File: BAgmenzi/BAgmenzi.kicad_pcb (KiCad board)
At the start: 6 copper layers, 66.2 x 44.8 mm, 146 parts, among them IC1 TPL0501-100RSER, J1 Conn_01x07, J2 DF52-2S-0.8H(21), J3 USB3076-30-A, J4 connector for CMUT, J5 3220-10-0100-00, Q1 NX7002BKMBYL, U1 MSP430FR5043IRGCT, U10 PESD1USB30, U11 MAX77654BENV+T, U13 TPS7A2033DBVDQN, U2 AD8338ACPZ-R7, U3 OPA836IDBVT, U4 OPA836IDBVT, U7 LT3463AEDD#PBF, U8 TPS22916CYFPR, U9 MAXM86161EFD_T, X1 FY0800018, X2 ABS07-32.768KHZ-9-T, Y1 AWSCR-8.00CV-T

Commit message: DRC correfted all red falgs
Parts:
- added TP2: vga_vref, TestPoint:TestPoint_Pad_D2.0mm, F.Cu at (192.8, 108.0)
- added TP6: TestPoint, TestPoint:TestPoint_Pad_D2.0mm, F.Cu at (192.8, 112.1)
- moved D4 1.02 mm to (127.6, 119.6)
- moved J3 0.78 mm to (122.5, 118.4)
- moved X2 0.54 mm to (125.6, 113.0)
- moved C16 0.53 mm to (123.9, 114.0)
- moved C18 0.52 mm to (123.9, 112.0)
- moved C50 0.46 mm to (150.5, 102.4), turned to 0 degrees
- moved R11 0.24 mm to (140.5, 95.7)
- moved X1 0.17 mm to (124.6, 118.4)
- moved C7 0.12 mm to (128.5, 109.2)
- moved R14 0.10 mm to (150.0, 116.4)
- turned R17 to 90 degrees
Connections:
- R17 pad 1: unconnected-(R17-Pad1) -> /TX/PULSER_IN
- R17 pad 2: unconnected-(R17-Pad2) -> PULSE_OUT
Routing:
- net GND: track 89.8 -> 137.5 mm, vias 67 -> 102
- net CHGIN: track 2.16 -> 45.1 mm, vias 0 -> 2
- net DVDD_3.3: track 56.1 -> 76.5 mm, vias 13 -> 23
- net PULSE_OUT: track 0.00 -> 17.7 mm, vias 0 -> 2
- net PULSER_HIZ_IN: track 0.99 -> 8.47 mm
- net Net-(C53-Pad1): track 0.40 -> 5.98 mm, vias 0 -> 2
- net /MSP/AVCC1: track 2.73 -> 5.85 mm
- net PPG_INT: track 81.1 -> 83.0 mm
- net DATA_READY: track 33.3 -> 31.6 mm
- net /TX/PULSER_EN: track 0.00 -> 1.65 mm
- net PPG_I2C.SCL: track 93.4 -> 94.9 mm
- net V_BAT: track 10.5 -> 9.26 mm, vias 3 -> 4
- net PMIC_IRQ: track 32.0 -> 33.2 mm
- net /MSP/LFXOUT: track 6.56 -> 5.44 mm
- net PPG_GPIO: track 66.0 -> 67.1 mm
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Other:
- board size 66.2 x 44.8 mm -> 64.7 x 44.8 mm

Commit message: added polyCMUT footprint, changed enables, more compact
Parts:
- removed J4: connector for CMUT, cmut_dummy:cmut-dummy
- removed TP2: vga_vref, TestPoint:TestPoint_Pad_D2.0mm
- removed TP6: TestPoint, TestPoint:TestPoint_Pad_D2.0mm
- added C67: 47u, Capacitor_SMD:C_0402_1005Metric, F.Cu at (146.6, 104.4)
- added R2: 1M, Resistor_SMD:R_0402_1005Metric, F.Cu at (144.3, 108.2)
- added R3: 1M, Resistor_SMD:R_0402_1005Metric, F.Cu at (142.9, 109.1)
- added R47: 1k, Resistor_SMD:R_0402_1005Metric, B.Cu at (125.5, 107.7)
- added R48: 1k, Resistor_SMD:R_0402_1005Metric, B.Cu at (124.5, 107.2)
- added U5: polyCMUT, polyCMUT:polyCMUT, F.Cu at (162.8, 108.8)
- C25: value 10nF -> 1.5n
- C34: value 1n -> 3.3n
- R10: value 100 -> 0
- R11: value 400 -> 1
- R7: value 2k -> 200
- R8: value 2k -> 1k
- moved R41 25.2 mm to (159.0, 95.7), turned to 180 degrees
- moved JP2 25.1 mm to (161.5, 97.9), turned to 90 degrees
- moved JP4 22.3 mm to (157.4, 97.6)
- moved R43 18.2 mm to (156.2, 99.7)
- moved C61 18.2 mm to (158.7, 99.7)
- moved R6 9.99 mm to (137.0, 115.1)
- moved C63 9.67 mm to (159.2, 120.9)
- moved JP5 9.67 mm to (157.4, 118.5)
- moved R44 9.67 mm to (155.9, 120.7)
- moved C62 9.67 mm to (157.7, 121.0)
- moved JP1 6.64 mm to (147.5, 118.3), turned to -90 degrees
- moved R30 4.88 mm to (166.3, 119.0)
- moved R29 4.84 mm to (166.3, 117.8)
- moved R27 4.39 mm to (169.4, 118.0)
- moved R28 4.24 mm to (169.4, 119.2)
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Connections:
- M1 pad F2: HV_PWR_EN -> Net-(M1-P115)
- M1 pad F3: VRX_EN -> Net-(M1-P114)
- M1 pad H5: HV_POS_EN -> BSL.UART_RX
- M1 pad H6: HV_NEG_EN -> BSL.UART_TX
- U1 pad 20: unconnected-(U1-P1.3_UCA1SOMI_UCA1RXD_TA1.1_A9_C9-Pad20) -> VRX_EN
- U1 pad 50: unconnected-(U1-P3.3_MCLK_TB0.3_XPB1-Pad50) -> HV_POS_EN
- U1 pad 51: unconnected-(U1-P3.4_SMCLK_DMAE0-Pad51) -> HV_NEG_EN
- U1 pad 52: unconnected-(U1-P3.5_ACLK_COUT-Pad52) -> HV_PWR_EN
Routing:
- net BSL.UART_TX: track 12.6 -> 38.6 mm, vias 0 -> 2
- net BSL.UART_RX: track 17.2 -> 40.8 mm, vias 0 -> 2
- net VRX_EN: track 32.8 -> 13.8 mm, vias 0 -> 1
- net HV_PWR_EN: track 43.1 -> 26.3 mm
- net HV_POS_EN: track 28.0 -> 12.5 mm, vias 0 -> 2
- net RX_IN: track 1.31 -> 14.5 mm
- net JTAG.RESET_N: track 29.6 -> 41.1 mm, vias 0 -> 2
- net Net-(M1-P115): track 0.00 -> 10.7 mm
- net PPG_I2C.SCL: track 94.9 -> 84.8 mm
- net HV_NEG_EN: track 27.3 -> 17.4 mm, vias 0 -> 2
- net JTAG.TEST: track 33.1 -> 42.8 mm, vias 0 -> 2
- net Net-(JP5-C): track 0.00 -> 9.40 mm
- net Net-(U1-CH1_OUT): track 0.00 -> 9.31 mm
- net Net-(M1-P114): track 0.00 -> 8.54 mm
- net Net-(U1-CH1_IN): track 0.00 -> 7.14 mm
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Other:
- board size 64.7 x 44.8 mm -> 64.8 x 44.8 mm

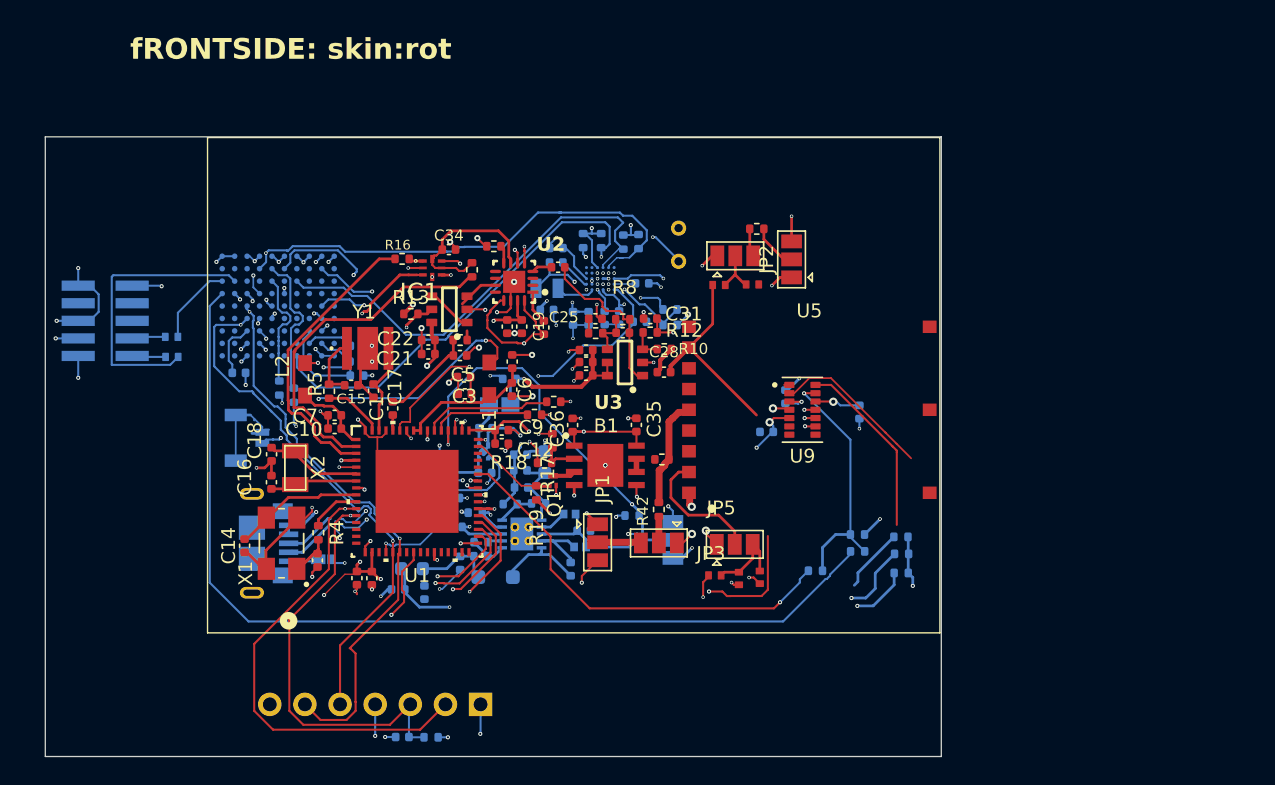
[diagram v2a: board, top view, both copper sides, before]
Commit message: part numbers added
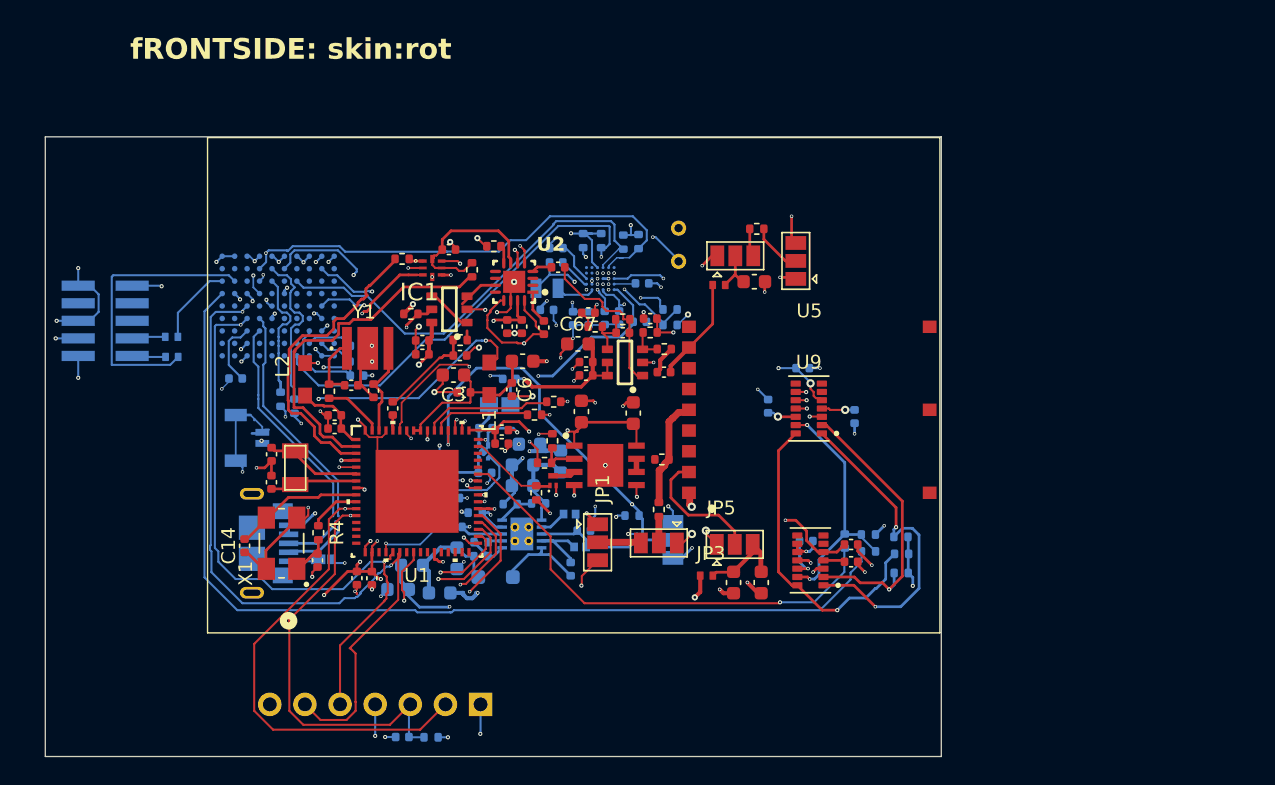
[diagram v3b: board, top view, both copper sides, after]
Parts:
- added C68: 1u, Capacitor_SMD:C_0402_1005Metric, F.Cu at (165.8, 119.8)
- added C69: 1u, Capacitor_SMD:C_0402_1005Metric, B.Cu at (162.6, 118.2)
- added C70: 10u, Capacitor_SMD:C_0402_1005Metric, F.Cu at (165.8, 118.5)
- added U6: DNP, MAXM86161EFD_T:PSON60P430X290X150-14N, F.Cu at (162.9, 119.7)
- C3, C35, C36, C37, C38, C4, C40, C41, C42, C43, C67: footprint Capacitor_SMD:C_0402_1005Metric -> Capacitor_SMD:C_0603_1608Metric
- C61, C62, C63: value 2.2U 50v -> 2.2u 50V; footprint EEG_PcbLib:0402 -> Capacitor_SMD:C_0603_1608Metric
- R18: value 1OK -> 10k
- R19, R36: value 10K -> 10k
- R41, R42, R43: value 100K -> 100k
- R71: renamed from R11oderC_direct1; value 0Ohm, oder 10nF 100V -> 0
- moved C46 6.61 mm to (159.8, 108.5), turned to -90 degrees
- moved C44 5.30 mm to (162.3, 105.8), turned to 180 degrees
- moved C45 5.20 mm to (166.1, 109.2), turned to 90 degrees
- moved R31 3.02 mm to (165.3, 118.2), turned to -90 degrees
- moved C36 1.17 mm to (146.3, 108.9)
- moved FB2 1.15 mm to (144.8, 112.5)
- moved C37 1.10 mm to (136.1, 122.0), turned to 0 degrees
- moved C42 1.01 mm to (142.6, 111.2)
- moved C35 0.88 mm to (150.1, 109.0)
- moved R48 0.81 mm to (124.5, 108.0)
- moved R47 0.79 mm to (125.5, 108.5)
- moved R29 0.79 mm to (167.1, 117.8)
- moved R30 0.79 mm to (167.1, 119.0)
- moved C3 0.77 mm to (137.1, 106.2)
- moved C4 0.76 mm to (142.1, 105.2), turned to 0 degrees
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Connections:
- M1 pad G3: unconnected-(M1-P128-PadG3) -> PPG_I2C.SDA
- M1 pad G8: PPG_I2C.SDA -> unconnected-(M1-P108-PadG8)
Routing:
- net PPG_I2C.SDA: track 73.5 -> 95.4 mm, vias 2 -> 3
- net BSL.UART_RX: track 40.8 -> 55.5 mm
- net GND: track 139.9 -> 151.6 mm, vias 99 -> 108
- net USB.D_N: track 27.3 -> 16.8 mm, vias 2 -> 0
- net USB.D_P: track 26.4 -> 16.0 mm, vias 2 -> 0
- net PPG_I2C.SCL: track 84.8 -> 92.7 mm
- net BSL.UART_TX: track 38.6 -> 46.3 mm
- net RX_IN: track 14.5 -> 7.56 mm
- net V_LED: track 8.93 -> 15.3 mm, vias 4 -> 5
- net SPARE_PIN: track 30.6 -> 34.4 mm
- net Net-(JP5-B): track 5.95 -> 9.24 mm
- net Net-(U6-VREF): track 0.00 -> 3.12 mm, vias 0 -> 1
- net CHGIN: track 45.1 -> 47.7 mm
- net PPG_INT: track 78.6 -> 80.9 mm
- net PMIC_I2C.SCL: track 29.5 -> 27.4 mm
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
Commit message: LCSC parts complete, changed L5andL6 footprint
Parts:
- FB3: footprint PCB1:FP-BLM18-0_15-t0_8-IPC_A -> Inductor_SMD:L_0603_1608Metric
- L5, L6: footprint wulpus:INDC1005X45N -> wulpus_pro_acq:FP-LQH3NPH_ME-MFG
- R9: value 400 -> 402
- moved L6 1.85 mm to (146.6, 120.5)
- moved L5 1.56 mm to (146.3, 115.0)
- moved C33 1.23 mm to (144.3, 120.2)
- moved FB2 0.75 mm to (144.8, 111.8)
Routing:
- net /TX/+V_IN_HV: track 9.24 -> 14.4 mm
- net Net-(D2-K): track 6.34 -> 3.44 mm
- net Net-(U7-SW2): track 5.45 -> 3.83 mm
- net +HV: track 12.8 -> 14.1 mm
